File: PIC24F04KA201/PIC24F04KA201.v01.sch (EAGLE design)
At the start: 25 parts

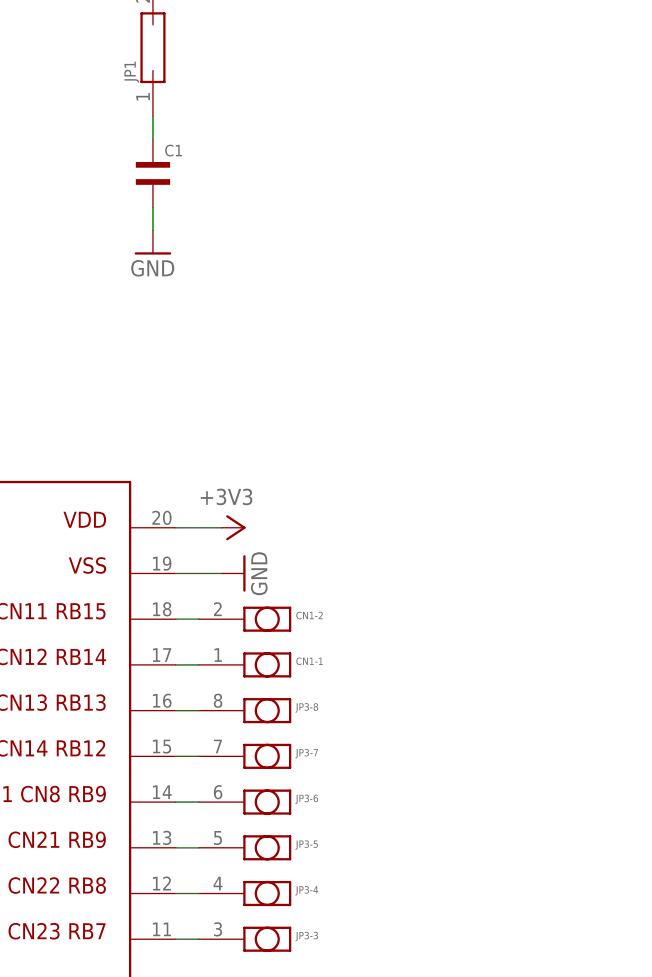
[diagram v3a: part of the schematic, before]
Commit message: Added dip8
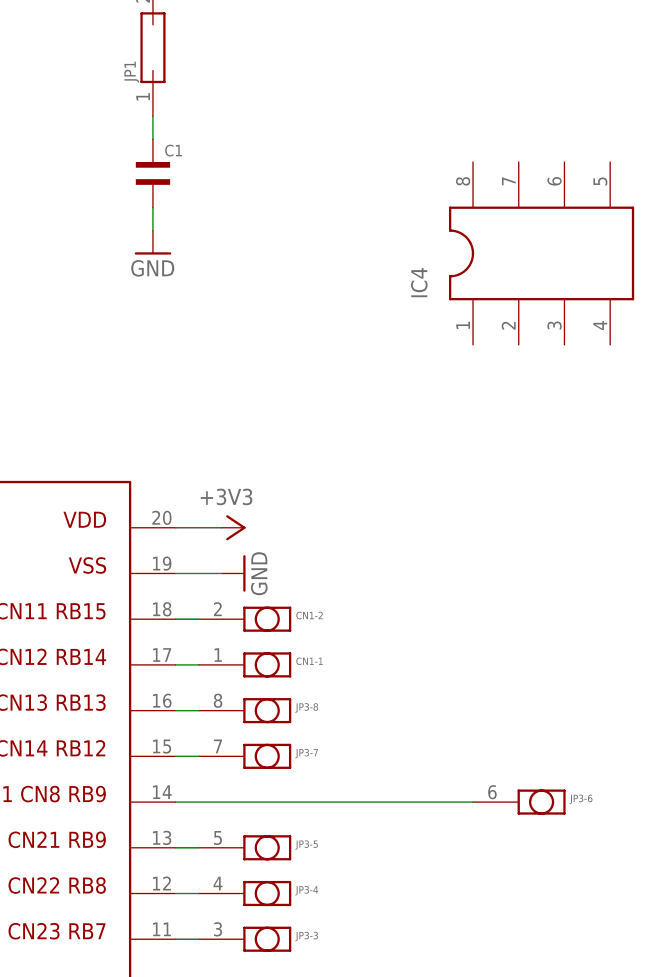
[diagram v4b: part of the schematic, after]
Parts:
- added IC4: (no value), SM-IC-Packages:DIP-08S
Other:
- moved on the sheet: JP3-6
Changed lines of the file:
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@@
 <part name="+3V6" library="supply1" deviceset="+3V3" device=""/>
 <part name="GND10" library="supply1" deviceset="GND" device=""/>
+<part name="IC4" library="SM-IC-Packages" deviceset="DIP-08" device="S"/>
 </parts>
 <sheets>
@@
 <instance part="JP3" gate="-4" x="58.42" y="-20.32"/>
 <instance part="JP3" gate="-5" x="58.42" y="-15.24"/>
-<instance part="JP3" gate="-6" x="58.42" y="-10.16"/>
+<instance part="JP3" gate="-6" x="88.9" y="-10.16"/>
 <instance part="JP3" gate="-7" x="58.42" y="-5.08"/>
 <instance part="JP3" gate="-8" x="58.42" y="0"/>
@@
 <instance part="+3V6" gate="G$1" x="60.96" y="20.32" rot="R270"/>
 <instance part="GND10" gate="1" x="60.96" y="15.24" rot="R90"/>
+<instance part="IC4" gate="G$1" x="93.98" y="50.8" rot="R90"/>
 </instances>
 <busses>
@@
 <pinref part="JP3" gate="-6" pin="P$1"/>
 <pinref part="IC1" gate="G$1" pin="P$14"/>
-<wire x1="55.88" y1="-10.16" x2="53.34" y2="-10.16" width="0.1524" layer="91"/>
-</segment>
-</net>
+<wire x1="86.36" y1="-10.16" x2="53.34" y2="-10.16" width="0.1524" layer="91"/>
+</segment>
+</net>
